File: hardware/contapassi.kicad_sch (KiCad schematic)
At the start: 0 parts

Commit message: Add new component models and scripts for schematic generation
- Added SOT-23-5 and SOT-23 models for components C14879 and C15127.
- Introduced WSON-8 model for component C97522.
- Created a script to assign electrical types to pins in generated symbols, ensuring accurate ERC checks.
- Developed a schematic generation script for the contapassi project, creating a netlist based on component connections.
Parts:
- added C1, C2: 18pF, Capacitor_SMD:C_0402_1005Metric, symbol Device:C
- added C10, C4, C5: 4.7uF, Capacitor_SMD:C_0603_1608Metric, symbol Device:C
- added C3: 47uF, Capacitor_SMD:C_1206_3216Metric, symbol Device:C
- added C6, C7, C8, C9: 100nF, Capacitor_SMD:C_0402_1005Metric, symbol Device:C
- added D1: PESD5V0S1BA, Diode_SMD:D_SOD-323, symbol Device:D_TVS
- added D2: rosso, LED_SMD:LED_0603_1608Metric, symbol Device:LED
- added J1: pogo pin, symbol Connector:Conn_01x02_Pin
- added J2: cella LiPo, symbol Connector:Conn_01x02_Pin
- added L1: 10uH, Inductor_SMD:L_0603_1608Metric, symbol Device:L
- added Q1: AO3401A, contapassi:SOT-23_L2.9-W1.3-P1.90-LS2.4-BR, symbol contapassi:AO3401A
- added R1, R2, R3, R4: 10k, Resistor_SMD:R_0402_1005Metric, symbol Device:R
- added R5, R8: 100k, Resistor_SMD:R_0402_1005Metric, symbol Device:R
- added R6: 20k, Resistor_SMD:R_0402_1005Metric, symbol Device:R
- added R7: 1k, Resistor_SMD:R_0402_1005Metric, symbol Device:R
- added TP1: SWDIO, symbol Connector:TestPoint
- added TP2: SWCLK, symbol Connector:TestPoint
- added TP3: GND, symbol Connector:TestPoint
- added TP4: +3V0, symbol Connector:TestPoint
- added TP5: RESET, symbol Connector:TestPoint
- added TP6: P0.04, symbol Connector:TestPoint
- added U1: E73-2G4M08S1C, contapassi:WIRELM-SMD_E73-2G4M08S1C, symbol contapassi:E73-2G4M08S1C
- added U2: LSM6DSV16XTR, contapassi:LGA-14_L3.0-W2.5-P0.50-BR, symbol contapassi:LSM6DSV16XTR
- added U3: W25Q256JVEIQ, contapassi:WSON-8_L8.0-W6.10-P1.27-BL-EP, symbol contapassi:W25Q256JVEIQTR
- added U4: MCP73831T-2ATI/OT, contapassi:SOT-23-5_L3.0-W1.7-P0.95-LS2.8-BR, symbol contapassi:MCP73831T-2ATI_OT
- added Y1: 32.768kHz, Crystal:Crystal_SMD_3215-2Pin_3.2x1.5mm, symbol Device:Crystal
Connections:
- new net +3V0: C5.1, C6.1, C7.1, C8.1, C9.1, L1.2, R1.1, R2.1, R3.1, R4.1, R5.1, TP4.1, U1.19 (VCC), U2.10 (OCS_Aux), U2.11 (SDO_Aux), U2.5 (Vdd_IO), U2.8 (Vdd), U3.8 (VCC)
- new net CHG_STAT: R5.2, U1.10 (AI6), U4.1 (STAT)
- new net CS_FLASH: R2.2, U1.20 (P12), U3.1 (~{CS})
- new net CS_IMU: R1.2, U1.22 (P0.07), U2.12 (CS)
- new net DCH: L1.1, U1.25 (DCH)
- new net FLASH_HOLD: R4.2, U3.7 (HOLD#orRESET#(IO3))
- new net FLASH_WP: R3.2, U3.3 (WP#(IO2))
- new net GND: C1.2, C10.2, C2.2, C3.2, C4.2, C5.2, C6.2, C7.2, C8.2, C9.2, D1.2 (A2), D2.2 (A), J1.2 (Pin_2), J2.2 (Pin_2), R6.2, R8.2, TP3.1, U1.21 (GND), U1.24 (GND), U1.5 (GND), U2.2 (SDx/AH1/Qvar1), U2.3 (SCx/AH2/Qvar2), U2.6 (GND), U2.7 (GND), U3.4 (GND), U3.9 (EP), U4.2 (VSS)
- new net IMU_INT1: U1.15 (AI3), U2.4 (INT1)
- new net IMU_INT2: U1.17 (P1.09), U2.9 (INT2)
- new net IPROG: R6.1, U4.5 (PROG)
- new net LED_A: D2.1 (K), R7.2
- new net LED_DRV: R7.1, U1.9 (AI7)
- new net RESET: TP5.1, U1.26 (RST)
- new net SPARE: TP6.1, U1.18 (AI2)
- new net SPI_MISO: U1.12 (P0.26), U2.1 (SDO/SA0), U3.2 (DO(IO1))
- new net SPI_MOSI: U1.14 (P0.06), U2.14 (SDA), U3.5 (DI(IO0))
- new net SPI_SCK: U1.16 (P0.08), U2.13 (SCL), U3.6 (CLK)
- new net SWCLK: TP2.1, U1.39 (SWC)
- new net SWDIO: TP1.1, U1.37 (SWD)
- new net VBAT: C3.1, C4.1, J2.1 (Pin_1), U1.23 (VDH), U4.3 (VBAT)
- new net VIN: D1.1 (A1), J1.1 (Pin_1), Q1.2 (S)
- new net VIN_GATE: Q1.1 (G), R8.1
- new net VIN_SW: C10.1, Q1.3 (D), U4.4 (VDD)
- new net XL1: C1.1, U1.11 (XL1), Y1.1
- new net XL2: C2.1, U1.13 (XL2), Y1.2
- no-connect marks 0 -> 22

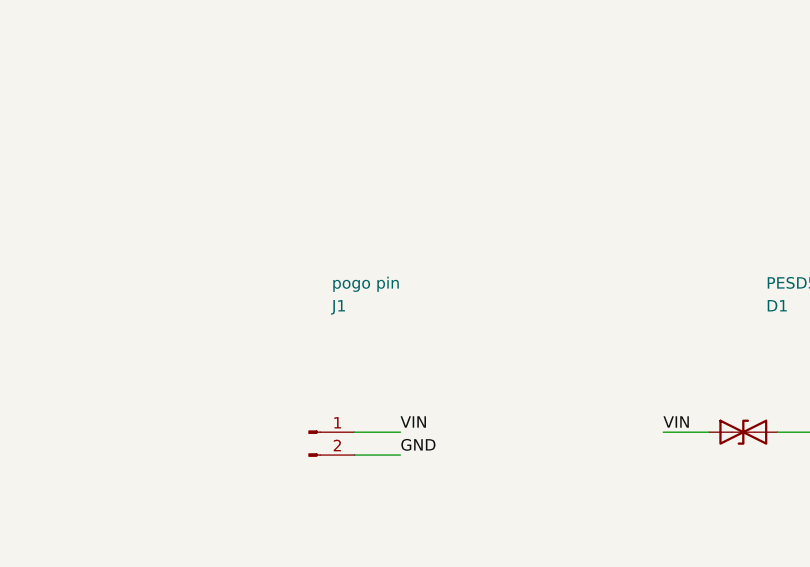
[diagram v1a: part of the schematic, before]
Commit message: Add scripts for generating PCB footprints and initial PCB layout
- Implemented gen_footprints.py to create footprints for pogo pads and battery cell connections.
- Implemented gen_pcb.py to generate the initial PCB layout, including component placement, keepout areas, and ground planes.
- Both scripts utilize a structured approach to ensure compatibility with KiCad and maintain clear documentation within the code.
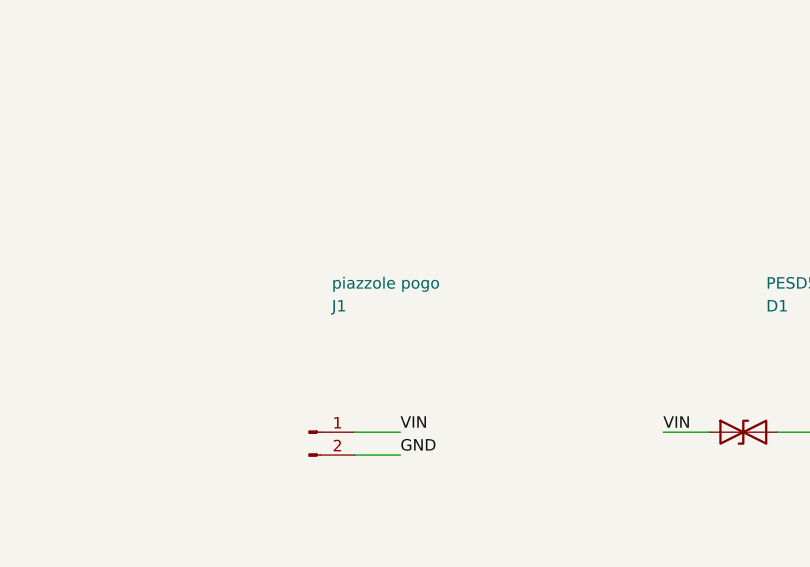
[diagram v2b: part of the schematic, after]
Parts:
- J1: value pogo pin -> piazzole pogo; footprint (none) -> contapassi:PogoPads_2P_P5.0mm
- J2: footprint (none) -> contapassi:CellPads_2P_P4.0mm
- TP1, TP2, TP3, TP4, TP5, TP6: footprint (none) -> TestPoint:TestPoint_Pad_1.5x1.5mm
